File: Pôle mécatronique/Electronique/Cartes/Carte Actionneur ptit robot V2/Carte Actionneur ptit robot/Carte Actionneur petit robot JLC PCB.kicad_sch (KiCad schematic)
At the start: 37 parts, among them Q1 BC557, U1 MCP2551-I-P

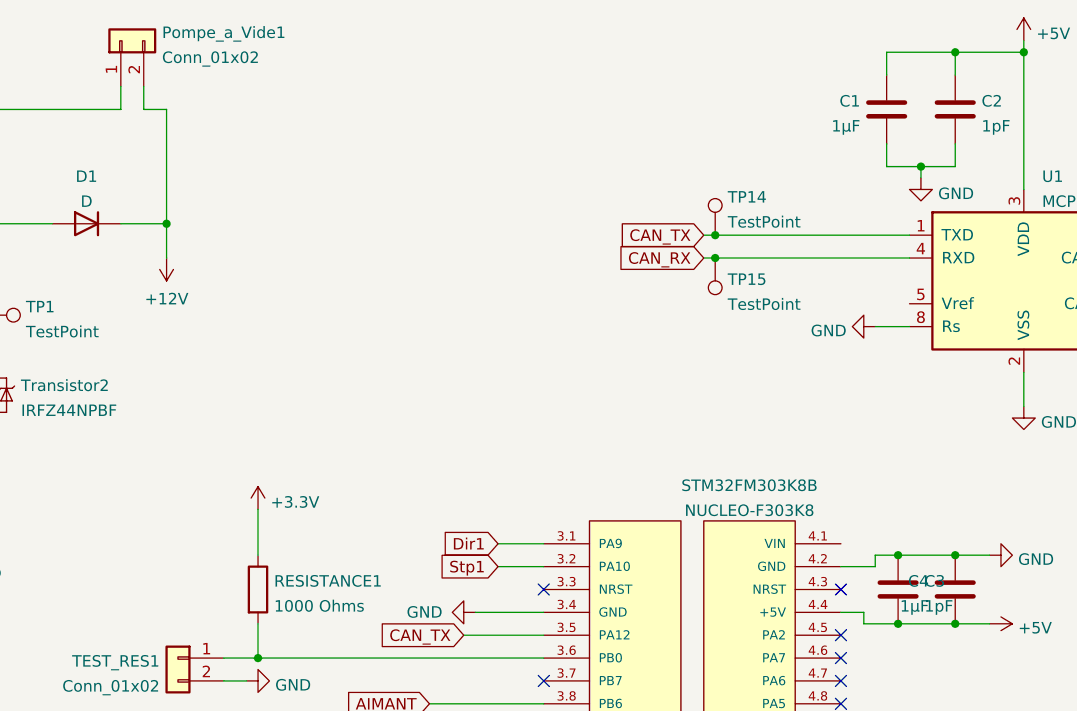
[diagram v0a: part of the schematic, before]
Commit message: Update actionneur grand robot
Ajout d'une 2e empreinte avec détrompeur
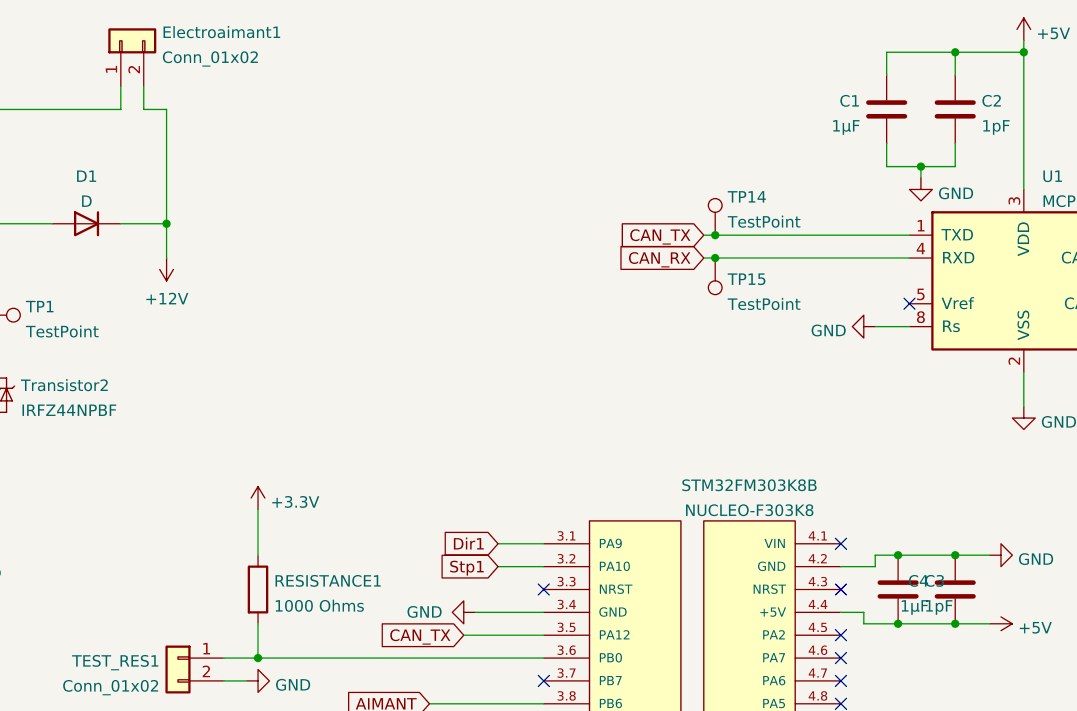
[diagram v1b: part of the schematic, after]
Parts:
- renumbered Pompe_a_Vide1 to Electroaimant1
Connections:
- no-connect marks 20 -> 22
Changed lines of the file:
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@@
   (no_connect (at 132.08 106.68))
   (no_connect (at 132.08 109.22))
+  (no_connect (at 165.1 73.66))
+  (no_connect (at 172.72 46.99))
   (no_connect (at 58.42 135.89))
   (no_connect (at 93.98 135.89))
@@
   (symbol (lib_id "Connector_Generic:Conn_01x02") (at 85.09 17.78 90) (unit 1)
     (in_bom yes) (on_board yes) (fields_autoplaced)
-    (property "Reference" "Pompe_a_Vide1" (id 0) (at 89.662 16.8715 90)
+    (property "Reference" "Electroaimant1" (id 0) (at 89.662 16.8715 90)
       (effects (font (size 1.27 1.27)) (justify right))
     )
@@
       (reference "DRIVER1") (unit 1) (value "TMC2208_SILENTSTEPSTICK") (footprint "MODULE_TMC2208_SILENTSTEPSTICK")
     )
+    (path "/6a1b1b3a-c86c-418d-8b46-56f6a0b7b240"
+      (reference "Electroaimant1") (unit 1) (value "Conn_01x02") (footprint "Connector_JST:JST_PH_B2B-PH-K_1x02_P2.00mm_Vertical")
+    )
     (path "/82dc1afd-1bfa-4473-8dd0-efbca2ee5fb0"
       (reference "MotPasAPas1") (unit 1) (value "Conn_01x04") (footprint "Connector_PinSocket_2.54mm:PinSocket_1x04_P2.54mm_Vertical")
     )
-    (path "/6a1b1b3a-c86c-418d-8b46-56f6a0b7b240"
-      (reference "Pompe_a_Vide1") (unit 1) (value "Conn_01x02") (footprint "Connector_JST:JST_PH_B2B-PH-K_1x02_P2.00mm_Vertical")
-    )
     (path "/7f158c77-240c-4d2a-bdf4-0faef377e7b5"
